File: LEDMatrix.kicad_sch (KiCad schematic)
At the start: 43 parts, among them J1 Conn_01x08, SW1 SW_Push, SW2 SW_Push, U1 W25Q80DVUXIE, U2 RP2040, Y1 ABLS-12.000MHZ-B4-T

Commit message: Schematic done, partially routed
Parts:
- removed C15: 100nF, Capacitor_SMD:C_0402_1005Metric, symbol Device:C
- removed J1: Conn_01x08, symbol Connector_Generic:Conn_01x08
- removed R4: 180k, Capacitor_SMD:C_0402_1005Metric, symbol Device:R_US
- removed SW1: SW_Push, symbol Switch:SW_Push
- removed U1: W25Q80DVUXIE, Package_SO:SOIC-8_5.23x5.23mm_P1.27mm, symbol Memory_Flash:W25Q128JVS
- removed Y1: ABLS-12.000MHZ-B4-T, RP2040_minimal:Crystal_SMD_HC49-US, symbol Device:Crystal
- added H1, H2: 24929, InputModule:MountingHole_3.7mm_Pad_24929, symbol Mechanical:MountingHole
- added H3, H4: MountingHole, MountingHole:MountingHole_2.1mm, symbol Mechanical:MountingHole
- added H5, H6, H7, H8: Tooling Hole, LEDMatrix:JLCPCB Tooling Hole, symbol Mechanical:MountingHole
- added J1: Conn_02x04_Odd_Even, InputModule:PogoPads_2x4_P2.0mm, symbol Connector_Generic:Conn_02x04_Odd_Even
- added R7: 330k, Resistor_SMD:R_0402_1005Metric, symbol Device:R_US
- added TP5: BOOTSEL, TestPoint:TestPoint_Pad_D1.0mm, symbol Connector:TestPoint
- added U1: W25Q16JVUXIQ, InputModule:SON-8-1EP_3x2mm_P0.5mm_EP0.2x1.6mm, symbol InputModule:W25Q16JVUX
- added Y1: 12.000MHz, Crystal:Crystal_SMD_3225-4Pin_3.2x2.5mm, symbol Device:Crystal_GND24
- C1, C2: value 27pF -> 15pF; Digikey (none) -> 490-5888-1-ND; LCSC (none) -> C1555; LCSC Alt (none) -> C1548; MANUFACTURER (none) -> Murata; MP (none) -> GRM1555C1H150JA01D
- C10, C11, C4, C5, C7, C9: Digikey (none) -> 1276-1001-1-ND; LCSC (none) -> C1525
- C12: renamed from C13; Digikey (none) -> 1276-1001-1-ND; LCSC (none) -> C1525
- C13: renamed from C14; Digikey (none) -> 1276-1001-1-ND; LCSC (none) -> C1525
- C14: renamed from C12; footprint Capacitor_SMD:C_0805_2012Metric -> Capacitor_SMD:C_0402_1005Metric; Digikey (none) -> 1276-1001-1-ND; LCSC (none) -> C1525
- C15: renamed from C23; footprint Capacitor_SMD:C_0805_2012Metric -> Capacitor_SMD:C_0603_1608Metric; Digikey (none) -> 1276-1869-1-ND; LCSC (none) -> C96446
- C16: footprint Capacitor_SMD:C_0805_2012Metric -> Capacitor_SMD:C_0603_1608Metric; Digikey (none) -> 1276-1869-1-ND; LCSC (none) -> C96446
- C3: Digikey (none) -> 1276-1001-1-ND; LCSC (none) -> C1525; MANUFACTURER (none) -> Samsung; MP (none) -> CL05B104KO5NNNC
- C6, C8: Digikey (none) -> 1276-1445-1-ND; LCSC (none) -> C52923
- D1, D2, D3, D4, D5: footprint (none) -> Diode_SMD:D_0402_1005Metric; Digikey (none) -> F9744CT-ND; LCSC (none) -> C468904
- R1, R3: footprint Capacitor_SMD:C_0402_1005Metric -> Resistor_SMD:R_0402_1005Metric; Digikey (none) -> 311-1.00KLRCT-ND; LCSC (none) -> C11702; MANUFACTURER (none) -> Yageo; MP (none) -> RC0402FR-071KL
- R10, R11, R8, R9: footprint Capacitor_SMD:C_0402_1005Metric -> Resistor_SMD:R_0402_1005Metric
- R2: value DNF -> 10k; footprint Capacitor_SMD:C_0402_1005Metric -> Resistor_SMD:R_0402_1005Metric; now left out of the parts list
- R4: renamed from R5; value DNF -> 10k; footprint Capacitor_SMD:C_0402_1005Metric -> Resistor_SMD:R_0402_1005Metric
- R5: renamed from R6; footprint Capacitor_SMD:C_0402_1005Metric -> Resistor_SMD:R_0402_1005Metric; Digikey (none) -> P27.0LCT-ND; LCSC (none) -> C138021
- R6: renamed from R7; footprint Capacitor_SMD:C_0402_1005Metric -> Resistor_SMD:R_0402_1005Metric; Digikey (none) -> P27.0LCT-ND; LCSC (none) -> C138021
- SW2: footprint (none) -> Button_Switch_SMD:SW_SPST_CK_KXT3
- TP1, TP2, TP3, TP4: footprint (none) -> TestPoint:TestPoint_Pad_D1.0mm
- U2: footprint RP2040_minimal:RP2040-QFN-56 -> Package_DFN_QFN:QFN-56-1EP_7x7mm_P0.4mm_EP3.2x3.2mm; Digikey (none) -> 2648-SC0914(13)CT-ND; LCSC (none) -> C2040
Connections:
- net ~{USB_BOOT} is gone; now on net QSPI_SS: R1.2
- net +3V3: now also D1.1 (A1), J1.8 (Pin_8), U1.8 (VCC); no longer D2.1 (A1)
- net +5V: now also D2.1 (A1), J1.2 (Pin_2); no longer D1.1 (A1)
- net BOARD_ID: now also J1.4 (Pin_4), R7.1
- net GND: now also C1.1, C2.1, J1.1 (Pin_1), J1.7 (Pin_7), R7.2, U1.4 (GND), U1.9 (EP), Y1.2, Y1.4; no longer C1.2, C2.2
- net QSPI_SCLK: now also U1.6 (CLK)
- net QSPI_SD0: now also U1.5 (DI(IO0))
- net QSPI_SD1: now also U1.2 (DO(IO1))
- net QSPI_SD2: now also U1.3 (IO2)
- net QSPI_SD3: now also U1.7 (IO3)
- net QSPI_SS: now also U1.1 (~{CS}); no longer R1.1
- net XIN: now also C1.2, Y1.3; no longer C1.1
- net XOUT: now also R3.2; no longer R3.1
- net ~{SLEEP}: now also J1.6 (Pin_6)
- net USB_D+ renamed USB_DP
- net USB_DP: now also J1.5 (Pin_5)
- net USB_D- renamed USB_DN
- net USB_DN: now also J1.3 (Pin_3)
- new net: R1.1, TP5.1
- new net: C2.2, R3.1, Y1.1
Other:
- note added: "SPI Flash"
- note removed: "Flash"
- note removed: "ZIF Header"
- moved on the sheet: TP1, TP2, TP3, TP4

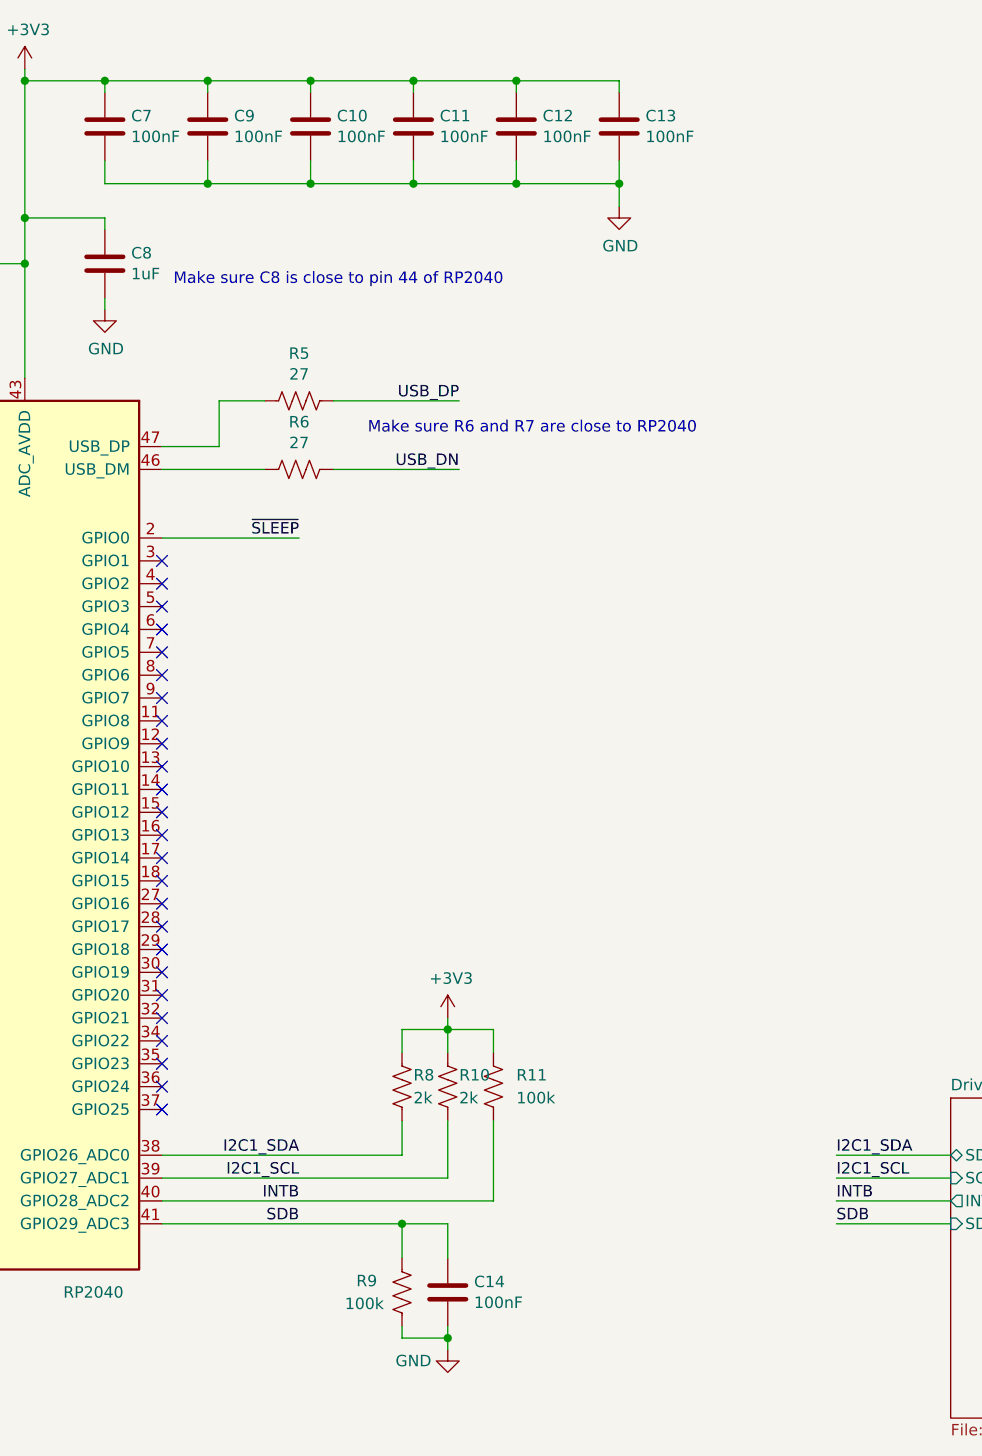
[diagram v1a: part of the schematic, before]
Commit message: Routing complete but not DRC clean
Also want to add 3-9 neopixels here to backlight the legend.
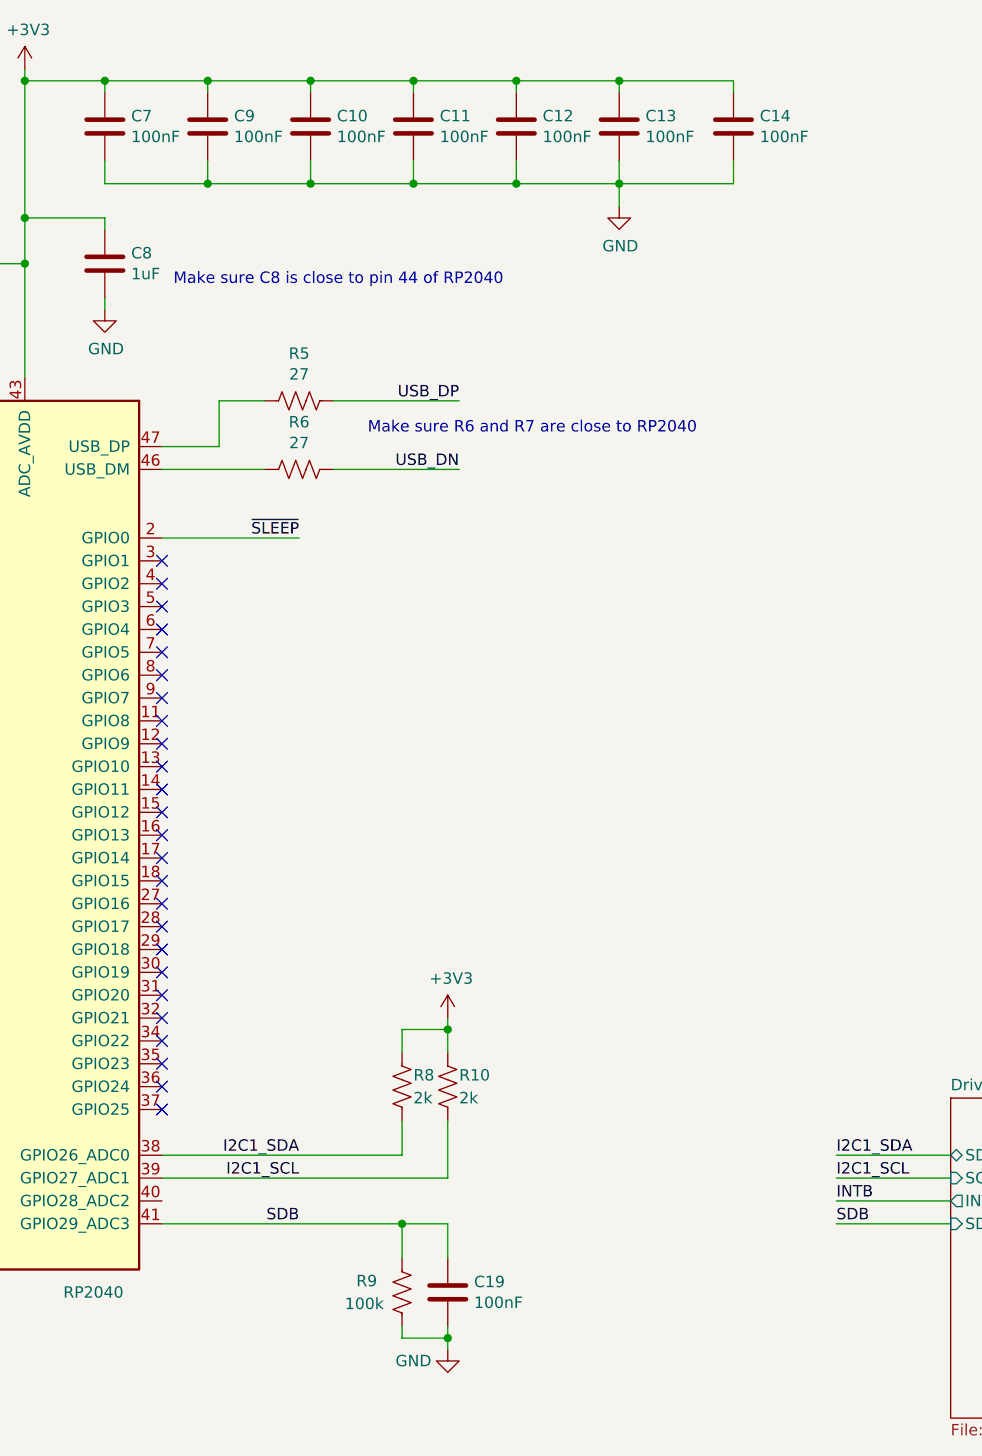
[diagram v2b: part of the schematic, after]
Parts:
- removed R11: 100k, Resistor_SMD:R_0402_1005Metric, symbol Device:R_US
- added C14: 100nF, Capacitor_SMD:C_0402_1005Metric, symbol Device:C
- renumbered C14 to C19
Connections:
- net +3V3: now also C14.1
- net GND: now also C14.2
- net INTB: no longer U2.40 (GPIO28_ADC2)
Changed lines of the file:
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@@
 	)
 	(junction
+		(at 275.59 21.59)
+		(diameter 0)
+		(color 0 0 0 0)
+	)
+	(junction
 		(at 190.5 224.79)
 		(diameter 0)
@@
 	(wire
 		(pts
-			(xy 147.32 107.95) (xy 161.29 107.95)
+			(xy 288.29 30.48) (xy 288.29 33.02)
 		)
 		(stroke
@@
 	(wire
 		(pts
-			(xy 33.02 30.48) (xy 26.67 30.48)
+			(xy 147.32 107.95) (xy 161.29 107.95)
 		)
 		(stroke
@@
 	(wire
 		(pts
-			(xy 261.62 127) (xy 261.62 129.54)
+			(xy 33.02 30.48) (xy 26.67 30.48)
 		)
 		(stroke
@@
 	(wire
 		(pts
-			(xy 256.54 127) (xy 261.62 127)
-		)
-		(stroke
-			(width 0)
-			(type default)
-		)
-	)
-	(wire
-		(pts
 			(xy 50.8 138.43) (xy 57.15 138.43)
 		)
@@
 	(wire
 		(pts
-			(xy 243.84 64.77) (xy 257.81 64.77)
+			(xy 275.59 21.59) (xy 288.29 21.59)
 		)
 		(stroke
@@
 	(wire
 		(pts
-			(xy 264.16 30.48) (xy 264.16 33.02)
+			(xy 243.84 64.77) (xy 257.81 64.77)
 		)
 		(stroke
@@
 	(wire
 		(pts
-			(xy 201.93 41.91) (xy 205.74 41.91)
+			(xy 264.16 30.48) (xy 264.16 33.02)
 		)
 		(stroke
@@
 	(wire
 		(pts
-			(xy 194.31 54.61) (xy 194.31 41.91)
+			(xy 201.93 41.91) (xy 205.74 41.91)
 		)
 		(stroke
@@
 	(wire
 		(pts
-			(xy 251.46 148.59) (xy 256.54 148.59)
+			(xy 194.31 54.61) (xy 194.31 41.91)
 		)
 		(stroke
@@
 	(wire
 		(pts
-			(xy 218.44 22.86) (xy 218.44 21.59)
+			(xy 251.46 148.59) (xy 256.54 148.59)
 		)
 		(stroke
@@
 	(wire
 		(pts
-			(xy 256.54 127) (xy 256.54 129.54)
+			(xy 218.44 22.86) (xy 218.44 21.59)
 		)
 		(stroke
@@
 	(wire
 		(pts
-			(xy 55.88 173.99) (xy 55.88 175.26)
+			(xy 256.54 127) (xy 256.54 129.54)
 		)
 		(stroke
@@
 	(wire
 		(pts
-			(xy 224.79 146.05) (xy 261.62 146.05)
+			(xy 55.88 173.99) (xy 55.88 175.26)
 		)
 		(stroke
@@
 	(wire
 		(pts
+			(xy 288.29 21.59) (xy 288.29 22.86)
+		)
+		(stroke
+			(width 0)
+			(type default)
+		)
+	)
+	(wire
+		(pts
 			(xy 184.15 41.91) (xy 189.23 41.91)
 		)
@@
 	(wire
 		(pts
-			(xy 261.62 137.16) (xy 261.62 146.05)
-		)
-		(stroke
-			(width 0)
-			(type default)
-		)
-	)
-	(wire
-		(pts
 			(xy 135.89 135.89) (xy 135.89 138.43)
 		)
@@
 	(wire
 		(pts
+			(xy 288.29 33.02) (xy 275.59 33.02)
+		)
+		(stroke
+			(width 0)
+			(type default)
+		)
+	)
+	(wire
+		(pts
 			(xy 212.09 222.25) (xy 212.09 224.79)
 		)
@@
 		)
 	)
-	(label "INTB"
-		(at 240.03 146.05 180)
-		(fields_autoplaced yes)
-		(effects
-			(font
-				(size 1.27 1.27)
-			)
-			(justify right bottom)
-		)
-	)
 	(label "~{SLEEP}"
 		(at 66.04 233.68 180)
@@
 	)
 	(symbol
+		(lib_id "Device:C")
+		(at 288.29 26.67 0)
+		(unit 1)
+		(exclude_from_sim no)
+		(in_bom yes)
+		(on_board yes)
+		(dnp no)
+		(property "Reference" "C14"
+			(at 291.211 25.5016 0)
+			(effects
+				(font
+					(size 1.27 1.27)
+				)
+				(justify left)
+			)
+		)
+		(property "Value" "100nF"
+			(at 291.211 27.813 0)
+			(effects
+				(font
+					(size 1.27 1.27)
+				)
+				(justify left)
+			)
+		)
+		(property "Footprint" "Capacitor_SMD:C_0402_1005Metric"
+			(at 289.2552 30.48 0)
+			(effects
+				(font
+					(size 1.27 1.27)
+				)
+				(hide yes)
+			)
+		)
+		(property "Datasheet" "~"
+			(at 288.29 26.67 0)
+			(effects
+				(font
+					(size 1.27 1.27)
+				)
+				(hide yes)
+			)
+		)
+		(property "Description" "Unpolarized capacitor"
+			(at 288.29 26.67 0)
+			(effects
+				(font
+					(size 1.27 1.27)
+				)
+				(hide yes)
+			)
+		)
+		(property "Digikey" "1276-1001-1-ND"
+			(at 288.29 26.67 0)
+			(effects
+				(font
+					(size 1.27 1.27)
+				)
+				(hide yes)
+			)
+		)
+		(property "LCSC" "C1525"
+			(at 288.29 26.67 0)
+			(effects
+				(font
+					(size 1.27 1.27)
+				)
+				(hide yes)
+			)
+		)
+		(pin "1"
+		)
+		(pin "2"
+		)
+		(instances
+			(project "LEDMatrix"
+				(path "/2fa7b4ce-e682-4c2e-9419-b1318fe8c56d"
+					(reference "C14")
+					(unit 1)
+				)
+			)
+		)
+	)
+	(symbol
 		(lib_id "power:+5V")
 		(at 166.37 212.09 0)
@@
 		(on_board yes)
 		(dnp no)
-		(property "Reference" "C14"
+		(property "Reference" "C19"
 			(at 259.461 155.0416 0)
 			(effects
@@
 			(project "LEDMatrix"
 				(path "/2fa7b4ce-e682-4c2e-9419-b1318fe8c56d"
-					(reference "C14")
+					(reference "C19")
 					(unit 1)
 				)
@@
 					(unit 1)
 				)
-			)
-		)
-	)
-	(symbol
-		(lib_id "Device:R_US")
-		(at 261.62 133.35 0)
-		(unit 1)
-		(exclude_from_sim no)
-		(in_bom yes)
-		(on_board yes)
-		(dnp no)
-		(property "Reference" "R11"
-			(at 264.16 132.08 0)
-			(effects
-				(font
-					(size 1.27 1.27)
-				)
-				(justify left)
-			)
-		)
-		(property "Value" "100k"
-			(at 264.16 134.62 0)
-			(effects
-				(font
-					(size 1.27 1.27)
-				)
-				(justify left)
-			)
-		)
-		(property "Footprint" "Resistor_SMD:R_0402_1005Metric"
-			(at 262.636 133.604 90)
-			(effects
-				(font
-					(size 1.27 1.27)
-				)
-				(hide yes)
-			)
-		)
-		(property "Datasheet" "~"
-			(at 261.62 133.35 0)
-			(effects
-				(font
-					(size 1.27 1.27)
-				)
-				(hide yes)
-			)
-		)
-		(property "Description" "Resistor, US symbol"
-			(at 261.62 133.35 0)
-			(effects
-				(font
-					(size 1.27 1.27)
-				)
-				(hide yes)
-			)
-		)
-		(pin "1"
-		)
-		(pin "2"
-		)
-		(instances
-			(project "LEDMatrix"
-				(path "/2fa7b4ce-e682-4c2e-9419-b1318fe8c56d"
-					(reference "R11")
-					(unit 1)
-				)

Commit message: Finished version w/ legend on silkscreen, DRC clean
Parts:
- J1, SW2, TP1, TP2, TP3, TP4, TP5: now not fitted
- R10, R8: LCSC (none) -> C4109
- R2: LCSC (none) -> C25744; now in the parts list
- R4: LCSC (none) -> C25744
- R7: value 330k -> 180k; LCSC C23137 -> C25760
- R9: LCSC (none) -> C25741
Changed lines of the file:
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@@
 			)
 		)
+		(property "LCSC" "C4109"
+			(at 251.46 133.35 0)
+			(effects
+				(font
+					(size 1.27 1.27)
+				)
+				(hide yes)
+			)
+		)
 		(pin "1"
 		)
@@
 		(in_bom yes)
 		(on_board yes)
-		(dnp no)
+		(dnp yes)
 		(property "Reference" "TP1"
 			(at 44.45 130.81 90)
@@
 		(in_bom no)
 		(on_board yes)
-		(dnp no)
+		(dnp yes)
 		(property "Reference" "TP5"
 			(at 34.29 95.25 90)
@@
 		(in_bom yes)
 		(on_board yes)
-		(dnp no)
+		(dnp yes)
 		(property "Reference" "TP2"
 			(at 44.45 133.35 90)
@@
 		(in_bom yes)
 		(on_board yes)
-		(dnp no)
+		(dnp yes)
 		(fields_autoplaced yes)
 		(property "Reference" "SW2"
@@
 			)
 		)
-		(property "Value" "330k"
+		(property "Value" "180k"
 			(at 76.2 233.68 90)
 			(effects
@@
 			)
 		)
-		(property "LCSC" "C23137"
+		(property "LCSC" "C25760"
 			(at 73.66 231.14 0)
 			(effects
@@
 		(in_bom yes)
 		(on_board yes)
-		(dnp no)
+		(dnp yes)
 		(property "Reference" "TP4"
 			(at 44.45 138.43 90)
@@
 		(in_bom no)
 		(on_board yes)
-		(dnp no)
+		(dnp yes)
 		(fields_autoplaced yes)
 		(property "Reference" "J1"
@@
 			)
 		)
+		(property "LCSC" "C25741"
+			(at 251.46 156.21 0)
+			(effects
+				(font
+					(size 1.27 1.27)
+				)
+				(hide yes)
+			)
+		)
 		(pin "1"
 		)
@@
 		(in_bom yes)
 		(on_board yes)
-		(dnp no)
+		(dnp yes)
 		(property "Reference" "TP3"
 			(at 44.45 135.89 90)
@@
 			)
 		)
+		(property "LCSC" "C4109"
+			(at 256.54 133.35 0)
+			(effects
+				(font
+					(size 1.27 1.27)
+				)
+				(hide yes)
+			)
+		)
 		(pin "1"
 		)
@@
 		(unit 1)
 		(exclude_from_sim no)
-		(in_bom no)
+		(in_bom yes)
 		(on_board yes)
 		(dnp no)
@@
 			)
 		)
+		(property "LCSC" "C25744"
+			(at 52.07 73.66 0)
+			(effects
+				(font
+					(size 1.27 1.27)
+				)
+				(hide yes)
+			)
+		)
 		(pin "1"
 		)
@@
 			(at 135.89 115.57 0)
 			(effects
+				(font
+					(size 1.27 1.27)
+				)
+				(hide yes)
+			)
+		)
+		(property "LCSC" "C25744"
+			(at 135.89 115.57 0)
+			(effects
